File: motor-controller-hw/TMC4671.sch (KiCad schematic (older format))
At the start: 56 parts, among them J401 Trinamic_TRMI, J402 TMC4671 USART, U401 TMC4671, X401 IQXO-50

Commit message: Finished adding footprints to the schematic, started layout
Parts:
- J401: footprint (none) -> supermileage_footprints:DF20F-10DP-1V(56)
- X401: footprint Oscillator:Oscillator_SMD_IQD_IQXO70-4Pin_7.5x5.0mm -> supermileage_footprints:Clock-FOX924
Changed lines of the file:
@@
 F 0 "X401" H 2900 3000 50  0000 L CNN
 F 1 "IQXO-50" H 2900 3100 50  0000 L CNN
-F 2 "Oscillator:Oscillator_SMD_IQD_IQXO70-4Pin_7.5x5.0mm" H 3475 2375 50  0001 C CNN
+F 2 "supermileage_footprints:Clock-FOX924" H 3475 2375 50  0001 C CNN
 F 3 "https://www.foxonline.com/pdfs/fox924.pdf" H 2700 2700 50  0001 C CNN
 	1    2800 2700
@@
 F 0 "J401" H 1500 6467 50  0000 C CNN
 F 1 "Trinamic_TRMI" H 1500 6376 50  0000 C CNN
-F 2 "" H 1450 6050 50  0001 C CNN
+F 2 "supermileage_footprints:DF20F-10DP-1V(56)" H 1450 6050 50  0001 C CNN
 F 3 "~" H 1450 6050 50  0001 C CNN
 	1    1450 6050

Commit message: Moved chaged order of op-amps to make PCB layout easier. More pcb part positioning
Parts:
- TP401, TP402: footprint Connector_PinHeader_2.54mm:PinHeader_1x03_P2.54mm_Vertical -> Pin_Headers:Pin_Header_Straight_1x01_Pitch2.54mm
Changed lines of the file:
@@
 F 0 "TP401" V 1150 4450 50  0000 C CNN
 F 1 "B_Ref" V 1050 4250 50  0000 L CNN
-F 2 "Connector_PinHeader_2.54mm:PinHeader_1x03_P2.54mm_Vertical" H 1350 4150 50  0001 C CNN
+F 2 "Pin_Headers:Pin_Header_Straight_1x01_Pitch2.54mm" H 1350 4150 50  0001 C CNN
 F 3 "~" H 1350 4150 50  0001 C CNN
 	1    1150 4150
@@
 F 0 "TP402" V 2100 4450 50  0000 C CNN
 F 1 "A_Ref" V 2000 4250 50  0000 L CNN
-F 2 "Connector_PinHeader_2.54mm:PinHeader_1x03_P2.54mm_Vertical" H 2300 4150 50  0001 C CNN
+F 2 "Pin_Headers:Pin_Header_Straight_1x01_Pitch2.54mm" H 2300 4150 50  0001 C CNN
 F 3 "~" H 2300 4150 50  0001 C CNN
 	1    2100 4150

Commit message: Working PCB Layout
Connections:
- net Batt_Current: no longer C420.1, R409.2, TP422.2, U401.21 (AGPI_A)
- new net Batt_I: C420.1, R409.2, TP422.2, U401.21 (AGPI_A)
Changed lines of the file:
@@
 	9250 1050 9750 1050
 Text Label 7750 4500 2    50   ~ 0
-Batt_Current
+Batt_I
 Wire Wire Line
 	7750 4500 7200 4500
@@
 	9850 4950 9700 4950
 Text Label 8300 4950 0    50   ~ 0
-Batt_Current
+Batt_I
 Text Label 8300 5850 0    50   ~ 0
 Batt_V

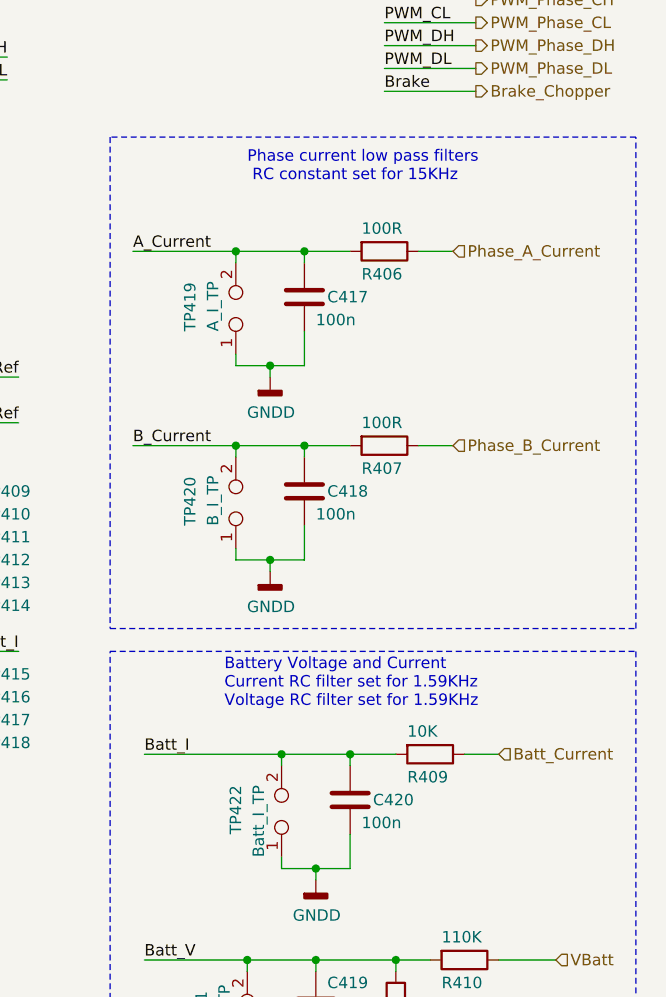
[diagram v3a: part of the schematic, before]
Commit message: Adding BOM, changed some footprints -Changed footprints to linux models in schematics -Added field Digi-key# to all components -Started filling in said field
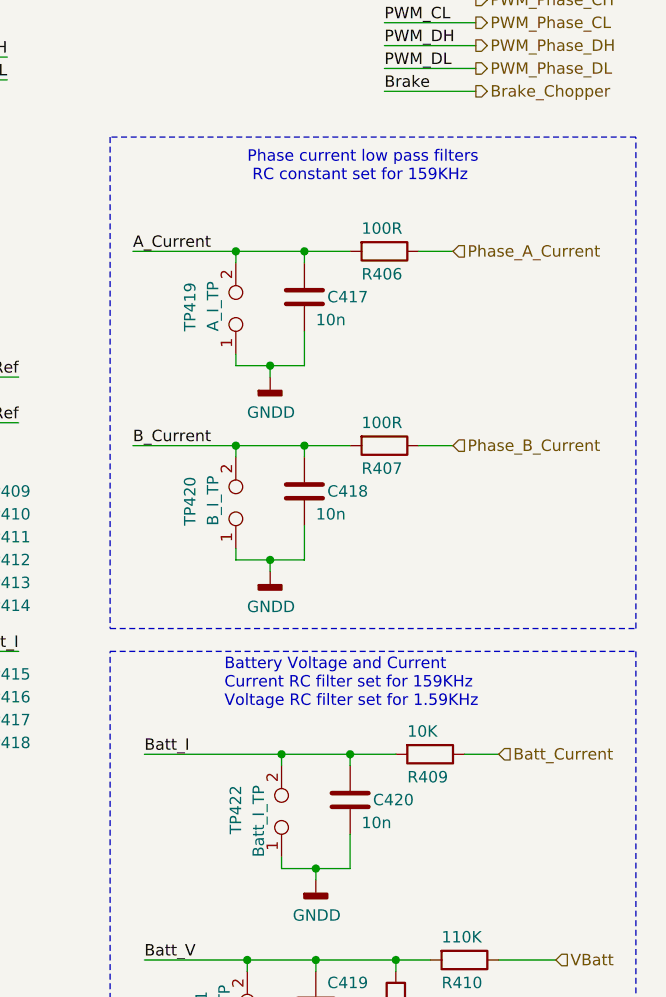
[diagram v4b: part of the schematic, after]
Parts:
- C401, C402, C403, C404, C405, C406, C407, C408, C409, C412, C413, C414, C415: footprint Capacitor_SMD:C_0805_2012Metric_Pad1.15x1.40mm_HandSolder -> Capacitors_SMD:C_0805_HandSoldering; Digi-key# (none) -> 1276-2444-1-ND
- C410: footprint Capacitor_SMD:C_0805_2012Metric_Pad1.15x1.40mm_HandSolder -> Capacitors_SMD:C_0805_HandSoldering; Digi-key# (none) -> 732-7670-1-ND
- C411, C416: footprint Capacitor_SMD:C_0805_2012Metric_Pad1.15x1.40mm_HandSolder -> Capacitors_SMD:C_0805_HandSoldering; Digi-key# (none) -> 732-7628-1-ND
- C417, C418, C420: value 100n -> 10n; footprint Capacitor_SMD:C_0805_2012Metric_Pad1.15x1.40mm_HandSolder -> Capacitors_SMD:C_0805_HandSoldering; Digi-key# (none) -> 732-12169-1-ND
- C419: footprint Capacitor_SMD:C_0805_2012Metric_Pad1.15x1.40mm_HandSolder -> Capacitors_SMD:C_0805_HandSoldering; Digi-key# (none) -> 732-12169-1-ND
- J401: Digi-key# (none) -> H10726CT-ND
- R401, R402, R403, R404, R405, R406, R407, R408, R409, R410: footprint Resistor_SMD:R_0805_2012Metric_Pad1.15x1.40mm_HandSolder -> Resistors_SMD:R_0805_HandSoldering
- U401: Digi-key# (none) -> 1460-1302-ND
- X401: Digi-key# (none) -> ‎631-1074-1-ND‎
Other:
- note added: "Battery Voltage and Current\nCurrent RC filter set for 159KHz\nVoltage RC filter set for 1.59KHz"
- note added: "Phase current low pass filters\n RC constant set for 159KHz"
- note removed: "Battery Voltage and Current\nCurrent RC filter set for 1.59KHz\nVoltage RC filter set for 1.59KHz"
- note removed: "Phase current low pass filters\n RC constant set for 15KHz"

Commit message: Added all of the digi-key part numbers
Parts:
- J402: Digi-key# (none) -> S1212EC-03-ND
- R401, R402, R403, R404, R405, R408, R409: Digi-key# (none) -> A129761CT-ND
- R406, R407: Digi-key# (none) -> 311-100CRCT-ND
- R410: Digi-key# (none) -> 311-110KCRCT-ND
- TP401, TP402, TP403, TP404, TP405, TP406, TP407, TP408, TP409, TP410, TP411, TP412, TP413, TP414, TP415, TP416, TP417, TP418, TP419, TP420, TP421, TP422: Digi-key# (none) -> N/A

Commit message: PCB rev 1.1 -Fixed the TMC4671 footprint (use the Digi-Key layout) -Fixed the USB pull up issue for using the DFU bootloader -Fixed the orientation of the Hall sensor connector -Added a PTC on the hall effect sensor line -Added a 5v jumper for the CAN port
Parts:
- U401: footprint supermileage_footprints:TMC4671 -> supermileage_footprints:QFN76P
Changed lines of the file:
@@
 F 0 "U401" H 5800 3500 50  0000 C CNN
 F 1 "TMC4671" H 5800 3600 50  0000 C CNN
-F 2 "supermileage_footprints:TMC4671" H 5800 3450 50  0001 C CNN
+F 2 "supermileage_footprints:QFN76P" H 5800 3450 50  0001 C CNN
 F 3 "https://www.trinamic.com/fileadmin/assets/Products/ICs_Documents/TMC4671_datasheet_v1.03.pdf" H 5800 3450 50  0001 C CNN
 F 4 "1460-1302-ND" H 5800 3450 50  0001 C CNN "Digi-key#"

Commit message: Power Stage Files Added
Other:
- note added: "SDE 4-30-19: TMC4671 hardware issue causes R408 to \nbe changed from 10K to 3.3K. The same issue necessitates the \naddition of a 10K resistor "piggiebacked" on C420."
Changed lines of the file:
@@
 Wire Wire Line
 	2100 4400 2100 4550
+Text Notes 7800 7050 0    50   ~ 0
+SDE 4-30-19: TMC4671 hardware issue causes R408 to \nbe changed from 10K to 3.3K. The same issue necessitates the \naddition of a 10K resistor "piggiebacked" on C420.
 $EndSCHEMATC
